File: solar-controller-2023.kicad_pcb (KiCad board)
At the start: 2 copper layers, 100 x 100 mm, 176 parts, among them J1 1-4, J2 5-8, J3 SWITCHES, J4 Debug, J5 USB_B, J6 SPI UP, J7 SPI DOWN, J8 USB_B, Q1 MMBT3906, Q2 DTC113Z, Q3 DTC113Z, Q4 DTC113Z, Q5 DTC113Z, Q6 DTC113Z, Q7 DTC113Z, Q8 DTC113Z, Q9 DTC113Z, SW1 ERASE, SW2 RESET, U1 ADG707, U10 AQH0213, U11 AQH0213, U12 AQH0213, U13 AQH0213, U14 AQH0213, U2 OPA2340, U3 OPA2340, U4 M95010, U5 SAM4S2A, U6 AP7381-33Y-13, U7 AQH0213, U8 AQH0213, U9 AQH0213, Y1 12M

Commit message: AC couple LMT01 signal conditioning and add gain
The difference circuit U3A was DC coupled and so could not
have gain.  Unit gain was only good for sensors up to 15m of
cat-5.
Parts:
- removed Q1: MMBT3906, Package_TO_SOT_SMD:SOT-23
- added C39: 680pF, Capacitor_SMD:C_0603_1608Metric_Pad1.08x0.95mm_HandSolder, F.Cu at (158.1, 79.8)
- added R45: 4K7, Resistor_SMD:R_0603_1608Metric_Pad0.98x0.95mm_HandSolder, F.Cu at (168.0, 69.9)
- C20: value 100nF -> 680pF
- R21, R22: value 10K -> 47K
- R24: value 4K7 -> 1K
- R26: value 10K -> 1K
- moved C20 10.4 mm to (163.2, 72.8)
- moved R26 6.80 mm to (163.7, 82.5), turned to 180 degrees
- moved R20 5.86 mm to (161.9, 79.8)
- moved R25 1.97 mm to (167.5, 82.5)
- moved R23 1.87 mm to (168.0, 68.0)
- moved C19 1.30 mm to (164.9, 72.8)
- moved U3 0.43 mm to (168.6, 74.8)
- moved R22 0.35 mm to (165.6, 79.8)
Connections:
- C20 pad 1: SENSOR_READY -> Net-(C20-Pad1)
- C20 pad 2: +3V3 -> Net-(U2-Pad6)
- J5 pad 2: Net-(J5-Pad1) -> /mcu/USB-
- R19 pad 1: Net-(R19-Pad1) -> Net-(C20-Pad1)
- R21 pad 1: Net-(R19-Pad2) -> Net-(R25-Pad2)
- R21 pad 2: GND -> Net-(R19-Pad2)
- R25 pad 1: SENSOR_TICK -> +3V3
- R25 pad 2: Net-(Q1-Pad1) -> Net-(R25-Pad2)
- R26 pad 1: SENSOR_READY -> Net-(R25-Pad2)
- R32 pad 2: Net-(J5-Pad1) -> /mcu/USB-
- U2 pad 1: Net-(R20-Pad1) -> Net-(U2-Pad1)
- U2 pad 2: Net-(R20-Pad1) -> Net-(U2-Pad1)
- U2 pad 6: Net-(R19-Pad1) -> Net-(U2-Pad6)
- U2 pad 7: Net-(R19-Pad1) -> Net-(U2-Pad6)
- U3 pad 5: Net-(R22-Pad2) -> Net-(R23-Pad2)
- U3 pad 6: Net-(R23-Pad2) -> Net-(R22-Pad2)
- U5 pad 26: SENSOR_READY -> unconnected-(U5-Pad26)
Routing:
- net /mcu/USB-: track 0.00 -> 47.7 mm
- net Net-(J5-Pad1): track 65.6 -> 17.9 mm
- net SENSOR_READY: track 39.4 -> 0.00 mm, vias 2 -> 0
- net Net-(R19-Pad1): track 11.6 -> 0.00 mm
- net Net-(U2-Pad6): track 0.00 -> 7.39 mm
- net Net-(R22-Pad2): track 16.6 -> 10.5 mm, vias 0 -> 2
- net Net-(R25-Pad2): track 0.00 -> 5.40 mm
- net Net-(R20-Pad2): track 14.9 -> 10.4 mm
- net Net-(U2-Pad1): track 0.00 -> 3.67 mm
- net Net-(R20-Pad1): track 5.07 -> 2.11 mm
- net Net-(C20-Pad1): track 0.00 -> 2.55 mm
- net GND: track 142.7 -> 140.4 mm
- net Net-(Q1-Pad1): track 2.28 -> 0.00 mm
- net SENSOR_TICK: track 62.2 -> 64.1 mm
- net Net-(R23-Pad2): track 4.38 -> 6.00 mm
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
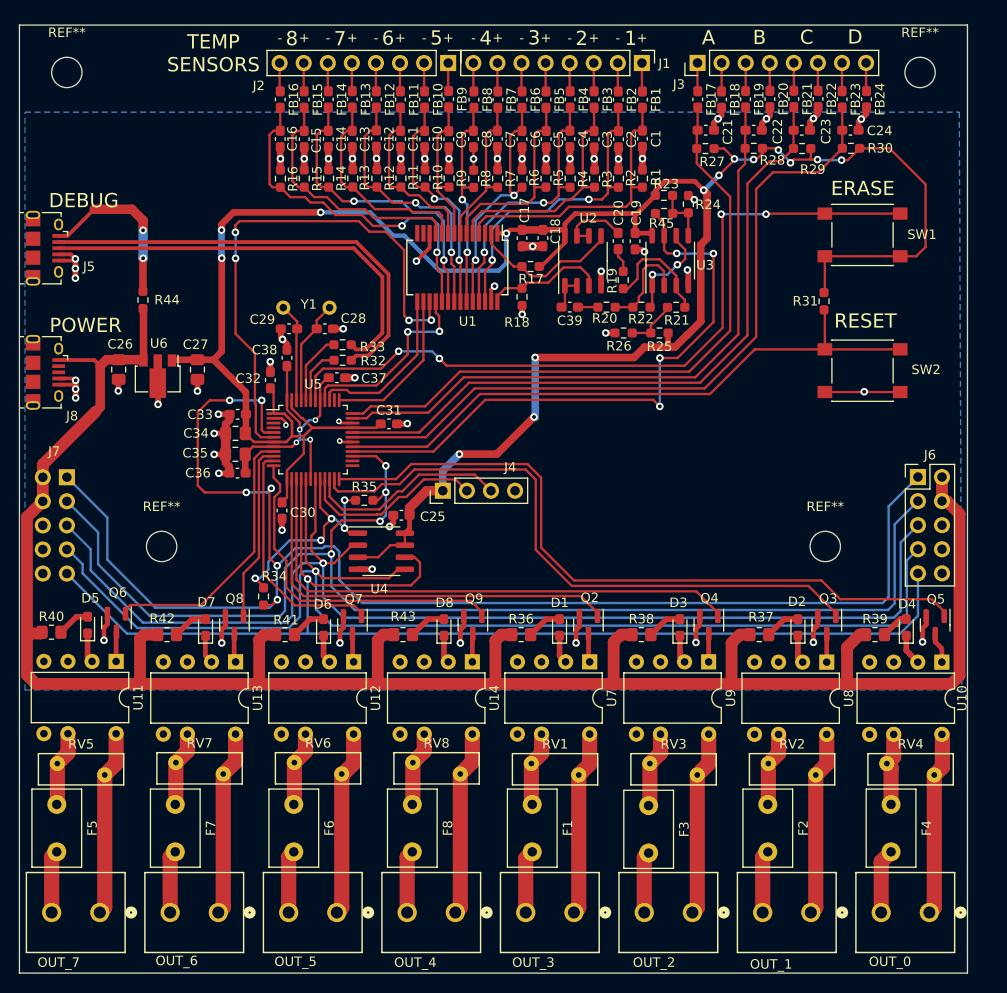
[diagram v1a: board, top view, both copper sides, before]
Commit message: replace sensor wire esd caps with TVSs
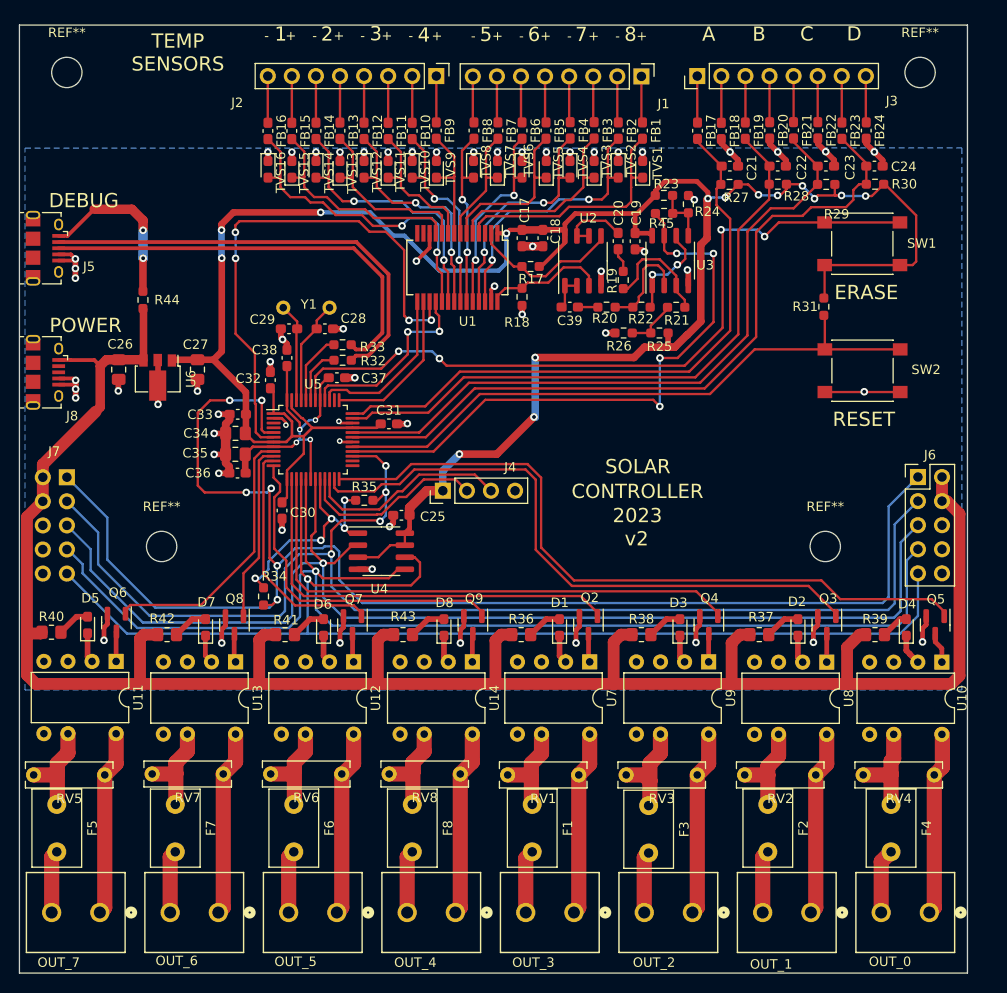
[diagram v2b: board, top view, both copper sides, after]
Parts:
- removed C1, C10, C11, C12, C13, C14, C15, C16, C2, C3, C4, C5, C6, C7, C8, C9: 1nF, Capacitor_SMD:C_0603_1608Metric_Pad1.08x0.95mm_HandSolder
- removed R1, R10, R11, R12, R13, R14, R15, R16, R2, R3, R4, R5, R6, R7, R8, R9: 47K, Resistor_SMD:R_0603_1608Metric_Pad0.98x0.95mm_HandSolder
- added TVS1: GG0603052, Diode_SMD:D_0603_1608Metric_Pad1.05x0.95mm_HandSolder, F.Cu at (165.7, 65.2)
- added TVS10: GG0603052, Diode_SMD:D_0603_1608Metric_Pad1.05x0.95mm_HandSolder, F.Cu at (141.4, 65.2)
- added TVS11: GG0603052, Diode_SMD:D_0603_1608Metric_Pad1.05x0.95mm_HandSolder, F.Cu at (138.9, 65.2)
- added TVS12: GG0603052, Diode_SMD:D_0603_1608Metric_Pad1.05x0.95mm_HandSolder, F.Cu at (136.3, 65.2)
- added TVS13: GG0603052, Diode_SMD:D_0603_1608Metric_Pad1.05x0.95mm_HandSolder, F.Cu at (133.8, 65.2)
- added TVS14: GG0603052, Diode_SMD:D_0603_1608Metric_Pad1.05x0.95mm_HandSolder, F.Cu at (131.3, 65.2)
- added TVS15: GG0603052, Diode_SMD:D_0603_1608Metric_Pad1.05x0.95mm_HandSolder, F.Cu at (128.7, 65.2)
- added TVS16: GG0603052, Diode_SMD:D_0603_1608Metric_Pad1.05x0.95mm_HandSolder, F.Cu at (126.2, 65.2)
- added TVS2: GG0603052, Diode_SMD:D_0603_1608Metric_Pad1.05x0.95mm_HandSolder, F.Cu at (163.2, 65.2)
- added TVS3: GG0603052, Diode_SMD:D_0603_1608Metric_Pad1.05x0.95mm_HandSolder, F.Cu at (160.6, 65.2)
- added TVS4: GG0603052, Diode_SMD:D_0603_1608Metric_Pad1.05x0.95mm_HandSolder, F.Cu at (158.1, 65.2)
- added TVS5: GG0603052, Diode_SMD:D_0603_1608Metric_Pad1.05x0.95mm_HandSolder, F.Cu at (155.6, 65.2)
- added TVS6: GG0603052, Diode_SMD:D_0603_1608Metric_Pad1.05x0.95mm_HandSolder, F.Cu at (153.0, 65.2)
- added TVS7: GG0603052, Diode_SMD:D_0603_1608Metric_Pad1.05x0.95mm_HandSolder, F.Cu at (150.4, 65.2)
- added TVS8: GG0603052, Diode_SMD:D_0603_1608Metric_Pad1.05x0.95mm_HandSolder, F.Cu at (147.9, 65.2)
- added TVS9: GG0603052, Diode_SMD:D_0603_1608Metric_Pad1.05x0.95mm_HandSolder, F.Cu at (144.0, 65.2)
- RV1, RV2, RV3, RV4, RV5, RV6, RV7, RV8: value V20E275PL1B1 -> B72214S0271K; footprint Varistor:RV_Disc_D9mm_W3.3mm_P5mm -> Capacitor_THT:C_Rect_L9.0mm_W2.5mm_P7.50mm_MKT
- U6: footprint Package_TO_SOT_SMD:SOT-89-3 -> Package_TO_SOT_SMD:SOT-89-3-JB
- moved R27 4.56 mm to (174.9, 66.8)
- moved C22 4.56 mm to (180.0, 64.9)
- moved R28 4.56 mm to (180.0, 66.8)
- moved R29 4.56 mm to (185.1, 66.8)
- moved R30 4.56 mm to (190.2, 66.8)
- moved C21 4.56 mm to (174.9, 64.9)
- moved C23 4.56 mm to (185.1, 64.9)
- moved C24 4.56 mm to (190.2, 64.9)
- moved FB11 3.56 mm to (138.9, 61.2)
- moved FB15 3.56 mm to (128.7, 61.2)
- moved FB16 3.56 mm to (126.2, 61.2)
- moved FB12 3.56 mm to (136.3, 61.2)
- moved FB10 3.56 mm to (141.4, 61.2)
- moved FB9 3.56 mm to (144.0, 61.1)
- moved FB13 3.56 mm to (133.8, 61.1)
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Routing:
- net GND: track 140.4 -> 120.5 mm
- net +3V3: track 255.7 -> 248.1 mm
- net Net-(FB6-Pad2): track 25.4 -> 21.0 mm
- net Net-(FB3-Pad2): track 25.1 -> 21.3 mm
- net Net-(FB2-Pad2): track 32.9 -> 29.1 mm
- net Net-(FB4-Pad2): track 28.9 -> 25.1 mm
- net Net-(FB7-Pad2): track 16.7 -> 12.9 mm
- net Net-(FB1-Pad2): track 30.1 -> 26.4 mm
- net Net-(FB8-Pad2): track 22.9 -> 19.2 mm
- net Net-(FB5-Pad2): track 21.4 -> 17.7 mm
- net Net-(F8-Pad1): track 7.93 -> 11.5 mm
- net Net-(FB9-Pad2): track 16.1 -> 12.7 mm
- net Net-(FB12-Pad2): track 28.9 -> 25.6 mm
- net Net-(FB11-Pad2): track 18.7 -> 15.4 mm
- net Net-(FB14-Pad2): track 32.6 -> 29.3 mm
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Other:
- board text added: "2023"
- board text added: "CONTROLLER"
- board text added: "SOLAR"
- board text added: "v2"

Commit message: generate gerbers
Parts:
- removed C18: 100nF, Capacitor_SMD:C_0603_1608Metric_Pad1.08x0.95mm_HandSolder
- removed U2: OPA2340, Package_SO:SOP-8_3.9x4.9mm_P1.27mm
- added C1: 10pF, Capacitor_SMD:C_0603_1608Metric_Pad1.08x0.95mm_HandSolder, F.Cu at (166.6, 83.3)
- added C2: 10pF, Capacitor_SMD:C_0603_1608Metric_Pad1.08x0.95mm_HandSolder, F.Cu at (162.8, 83.3)
- moved C20 8.45 mm to (156.0, 77.3), turned to 180 degrees
- moved R26 6.87 mm to (169.4, 78.6), turned to 90 degrees
- moved R23 6.61 mm to (170.9, 73.9), turned to 180 degrees
- moved R45 4.98 mm to (168.2, 74.8), turned to 90 degrees
- moved C19 4.50 mm to (160.8, 74.5)
- moved U3 4.50 mm to (164.5, 76.6)
- moved R20 4.29 mm to (157.8, 80.9)
- moved R19 3.91 mm to (159.8, 77.3), turned to 0 degrees
- moved R24 3.40 mm to (169.1, 72.0), turned to 0 degrees
- moved R22 3.28 mm to (162.9, 81.5), turned to 180 degrees
- moved R21 3.21 mm to (166.6, 81.5), turned to 180 degrees
- moved R27 2.59 mm to (172.3, 66.4)
- moved R28 2.59 mm to (177.4, 66.4)
- moved R29 2.59 mm to (182.5, 66.4)
- moved R30 2.59 mm to (187.7, 66.4)
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- renumbered REF** to MOUNT
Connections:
- C20 pad 2: Net-(U2-Pad6) -> Net-(R17-Pad2)
- C39 pad 2: Net-(U2-Pad1) -> Net-(R18-Pad2)
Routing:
- net Net-(R17-Pad2): track 16.8 -> 8.22 mm
- net Net-(U2-Pad6): track 7.39 -> 0.00 mm
- net Net-(R18-Pad2): track 12.9 -> 6.19 mm
- net GND: track 120.5 -> 114.9 mm, vias 62 -> 61
- net SW_3: track 78.2 -> 73.7 mm
- net Net-(U2-Pad1): track 3.67 -> 0.00 mm
- net SENSOR_TICK: track 64.1 -> 60.8 mm, vias 4 -> 2
- net SW_2: track 72.2 -> 69.1 mm
- net +3V3: track 248.1 -> 245.5 mm, vias 15 -> 12
- net SW_1: track 67.4 -> 65.3 mm
- net Net-(R19-Pad2): track 11.9 -> 10.3 mm
- net Net-(R20-Pad2): track 10.4 -> 11.7 mm
- net Net-(R22-Pad2): track 10.5 -> 11.7 mm
- net Net-(C20-Pad1): track 2.55 -> 2.04 mm
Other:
- board text added: "https://github.com/jbagg/solar-controller-2023-hw"
